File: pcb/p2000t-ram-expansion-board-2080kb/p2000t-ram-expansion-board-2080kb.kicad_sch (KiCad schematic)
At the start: 30 parts, among them J1 EXPANSION BOARD, J2 POWER, J3 TERMINAL, U1 74HC04, U10 AS6C4008-55PCN, U11 AS6C4008-55PCN, U12 74HC138, U13 74HC74, U2 AS6C4008-55PCN, U3 74HC00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

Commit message: Adding gerbers
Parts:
- added C14: 0.1uF, Capacitor_THT:C_Disc_D5.0mm_W2.5mm_P5.00mm, symbol Device:C
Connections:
- net +5V: now also C14.1
- net GND: now also C14.2
- no-connect marks 18 -> 17
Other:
- note added: "Currently not used"
- note added: "Port number 0x94 or 0x95 select D-type flip-flop 0x94 = 1001 0100 0x95 = 1001 0101"
- note added: "Writeable on port 0x94"
- note added: "Writeable on port 0x95"
- note removed: "Port number 0x94 selects D-type flip-flop 0x94 = 1001 0100"
- moved on the sheet: C2, U13A, U13B, U1A, U1D, U1E, U3B, U4, U6A

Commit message: Fixing bug in wiring
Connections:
- net A0: now also U3.4; no longer U1.11
- net GND: now also U1.11
- net at U1.10: no longer U3.4
- no-connect marks 17 -> 18
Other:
- note added: "0x94 | 0x95"
- note removed: "0x94"
- moved on the sheet: U1D, U1E
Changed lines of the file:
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@@
   (junction (at 113.03 85.09) (diameter 0) (color 0 0 0 0)
   )
+  (junction (at 91.44 53.975) (diameter 0) (color 0 0 0 0)
+  )
   (junction (at 93.98 59.055) (diameter 0) (color 0 0 0 0)
   )
@@
   )
   (no_connect (at 46.355 80.645))
+  (no_connect (at 144.78 224.79))
   (no_connect (at 237.49 163.195))
   (no_connect (at 33.655 75.565))
@@
     (stroke (width 0) (type default))
   )
-  (wire (pts (xy 217.17 51.435) (xy 217.17 46.355))
-    (stroke (width 0) (type default))
-  )
   (wire (pts (xy 239.395 109.855) (xy 239.395 123.19))
     (stroke (width 0) (type default))
@@
     (stroke (width 0) (type default))
   )
-  (wire (pts (xy 217.17 46.355) (xy 219.71 46.355))
-    (stroke (width 0) (type default))
-  )
   (polyline (pts (xy 200.66 89.535) (xy 177.165 89.535))
     (stroke (width 0) (type default))
@@
     (stroke (width 0) (type default))
   )
+  (wire (pts (xy 91.44 31.115) (xy 100.33 31.115))
+    (stroke (width 0) (type default))
+  )
   (wire (pts (xy 37.465 93.98) (xy 40.64 93.98))
     (stroke (width 0) (type default))
@@
     (stroke (width 0) (type default))
   )
-  (wire (pts (xy 234.95 38.1) (xy 234.95 46.355))
+  (wire (pts (xy 234.95 38.1) (xy 230.505 38.1))
     (stroke (width 0) (type default))
   )
@@
     (stroke (width 0) (type default))
   )
+  (wire (pts (xy 91.44 53.975) (xy 91.44 31.115))
+    (stroke (width 0) (type default))
+  )
   (wire (pts (xy 243.84 109.855) (xy 239.395 109.855))
     (stroke (width 0) (type default))
@@
     (effects (font (size 1.27 1.27)) (justify left bottom))
   )
-  (text "0x94" (at 90.678 64.516 90)
+  (text "0x94 | 0x95" (at 90.17 67.945 90)
     (effects (font (size 1.27 1.27)) (justify left bottom))
   )
@@
     )
   )
-  (global_label "A0" (shape input) (at 219.71 33.02 180) (fields_autoplaced)
+  (global_label "A0" (shape input) (at 234.95 33.02 180) (fields_autoplaced)
     (effects (font (size 1 1)) (justify right))
-    (property "Intersheetrefs" "${INTERSHEET_REFS}" (at 216.0005 32.9575 0)
+    (property "Intersheetrefs" "${INTERSHEET_REFS}" (at 231.2405 32.9575 0)
       (effects (font (size 1 1)) (justify right) hide)
     )
@@
     )
   )
-  (global_label "~{P=R}" (shape input) (at 217.17 51.435 270) (fields_autoplaced)
+  (global_label "~{P=R}" (shape input) (at 215.265 38.1 180) (fields_autoplaced)
     (effects (font (size 1.27 1.27)) (justify right))
-    (property "Intersheetrefs" "${INTERSHEET_REFS}" (at 217.17 58.5326 90)
+    (property "Intersheetrefs" "${INTERSHEET_REFS}" (at 208.1674 38.1 0)
       (effects (font (size 1.27 1.27)) (justify right) hide)
     )
@@
     )
   )
-  (symbol (lib_id "power:GND") (at 100.33 31.115 270) (unit 1)
-    (in_bom yes) (on_board yes) (dnp no) (fields_autoplaced)
-    (property "Reference" "#PWR065" (at 93.98 31.115 0)
-      (effects (font (size 1.27 1.27)) hide)
-    )
-    (property "Value" "GND" (at 96.52 31.115 90)
-      (effects (font (size 1.27 1.27)) (justify right))
-    )
-    (property "Footprint" "" (at 100.33 31.115 0)
-      (effects (font (size 1.27 1.27)) hide)
-    )
-    (property "Datasheet" "" (at 100.33 31.115 0)
-      (effects (font (size 1.27 1.27)) hide)
-    )
-    (pin "1")
-    (instances
-      (project "p2000t-ram-expansion-board-2080kb"
-        (path "/aa790391-403a-4556-8f28-ee78862c61e8"
-          (reference "#PWR065") (unit 1)
-        )
-      )
-    )
-  )
   (symbol (lib_id "power:GND") (at 291.465 60.96 180) (unit 1)
     (in_bom yes) (on_board yes) (dnp no) (fields_autoplaced)
@@
     )
   )
+  (symbol (lib_id "power:GND") (at 129.54 224.79 270) (unit 1)
+    (in_bom yes) (on_board yes) (dnp no)
+    (property "Reference" "#PWR071" (at 123.19 224.79 0)
+      (effects (font (size 1.27 1.27)) hide)
+    )
+    (property "Value" "GND" (at 121.92 224.79 90)
+      (effects (font (size 1.27 1.27)) (justify left))
+    )
+    (property "Footprint" "" (at 129.54 224.79 0)
+      (effects (font (size 1.27 1.27)) hide)
+    )
+    (property "Datasheet" "" (at 129.54 224.79 0)
+      (effects (font (size 1.27 1.27)) hide)
+    )
+    (pin "1")
+    (instances
+      (project "p2000t-ram-expansion-board-2080kb"
+        (path "/aa790391-403a-4556-8f28-ee78862c61e8"
+          (reference "#PWR071") (unit 1)
+        )
+      )
+    )
+  )
   (symbol (lib_id "74xx:74HC00") (at 242.57 35.56 0) (unit 2)
     (in_bom yes) (on_board yes) (dnp no)
@@
     )
   )
-  (symbol (lib_id "74xx:74HC04") (at 227.33 33.02 0) (unit 5)
+  (symbol (lib_id "74xx:74HC04") (at 137.16 224.79 0) (unit 5)
     (in_bom yes) (on_board yes) (dnp no)
-    (property "Reference" "U1" (at 220.98 36.195 0)
+    (property "Reference" "U1" (at 130.81 227.965 0)
       (effects (font (size 1.27 1.27)))
     )
-    (property "Value" "74HC04" (at 231.14 36.195 0)
+    (property "Value" "74HC04" (at 140.97 227.965 0)
       (effects (font (size 1.27 1.27)))
     )
-    (property "Footprint" "Package_DIP:DIP-14_W7.62mm_Socket" (at 227.33 33.02 0)
+    (property "Footprint" "Package_DIP:DIP-14_W7.62mm_Socket" (at 137.16 224.79 0)
       (effects (font (size 1.27 1.27)) hide)
     )
-    (property "Datasheet" "https://assets.nexperia.com/documents/data-sheet/74HC_HCT04.pdf" (at 227.33 33.02 0)
+    (property "Datasheet" "https://assets.nexperia.com/documents/data-sheet/74HC_HCT04.pdf" (at 137.16 224.79 0)
       (effects (font (size 1.27 1.27)) hide)
     )
@@
     )
   )
-  (symbol (lib_id "74xx:74HC04") (at 227.33 46.355 0) (unit 4)
+  (symbol (lib_id "74xx:74HC04") (at 222.885 38.1 0) (unit 4)
     (in_bom yes) (on_board yes) (dnp no)
-    (property "Reference" "U1" (at 220.98 42.545 0)
+    (property "Reference" "U1" (at 216.535 34.29 0)
       (effects (font (size 1.27 1.27)))
     )
-    (property "Value" "74HC04" (at 230.505 43.18 0)
+    (property "Value" "74HC04" (at 226.06 34.925 0)
       (effects (font (size 1.27 1.27)))
     )
-    (property "Footprint" "Package_DIP:DIP-14_W7.62mm_Socket" (at 227.33 46.355 0)
+    (property "Footprint" "Package_DIP:DIP-14_W7.62mm_Socket" (at 222.885 38.1 0)
       (effects (font (size 1.27 1.27)) hide)
     )
-    (property "Datasheet" "https://assets.nexperia.com/documents/data-sheet/74HC_HCT04.pdf" (at 227.33 46.355 0)
+    (property "Datasheet" "https://assets.nexperia.com/documents/data-sheet/74HC_HCT04.pdf" (at 222.885 38.1 0)
       (effects (font (size 1.27 1.27)) hide)
     )

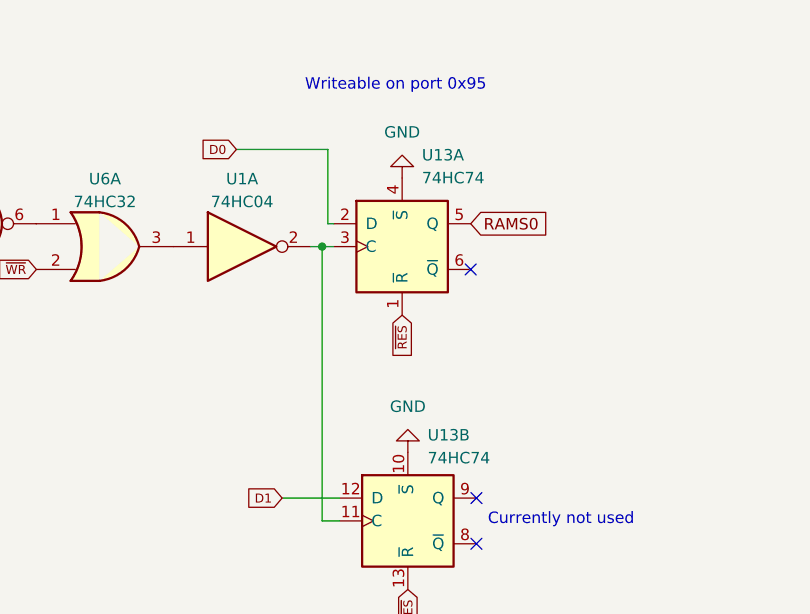
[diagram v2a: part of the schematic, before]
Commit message: Fixing another bug 74HC74
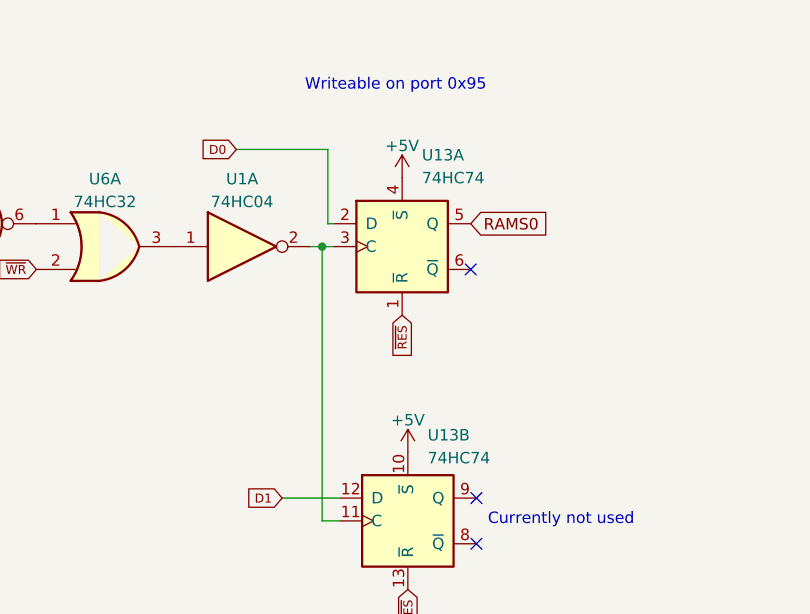
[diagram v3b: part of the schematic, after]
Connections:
- net +5V: now also U13.10 (~{S}), U13.4 (~{S})
- net GND: no longer U13.10 (~{S}), U13.4 (~{S})
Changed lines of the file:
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@@
-    )
-  )
-  (symbol (lib_id "power:GND") (at 291.465 60.96 180) (unit 1)
-    (in_bom yes) (on_board yes) (dnp no) (fields_autoplaced)
-    (property "Reference" "#PWR066" (at 291.465 54.61 0)
-      (effects (font (size 1.27 1.27)) hide)
-    )
-    (property "Value" "GND" (at 291.465 55.88 0)
-      (effects (font (size 1.27 1.27)))
-    )
-    (property "Footprint" "" (at 291.465 60.96 0)
-      (effects (font (size 1.27 1.27)) hide)
-    )
-    (property "Datasheet" "" (at 291.465 60.96 0)
-      (effects (font (size 1.27 1.27)) hide)
-    )
-    (pin "1")
-    (instances
-      (project "p2000t-ram-expansion-board-2080kb"
-        (path "/aa790391-403a-4556-8f28-ee78862c61e8"
-          (reference "#PWR066") (unit 1)
-        )
-      )
     )
   )
@@
         (path "/aa790391-403a-4556-8f28-ee78862c61e8"
           (reference "#PWR02") (unit 1)
-        )
-      )
-    )
-  )
-  (symbol (lib_id "power:GND") (at 290.83 30.48 180) (unit 1)
-    (in_bom yes) (on_board yes) (dnp no) (fields_autoplaced)
-    (property "Reference" "#PWR064" (at 290.83 24.13 0)
-      (effects (font (size 1.27 1.27)) hide)
-    )
-    (property "Value" "GND" (at 290.83 25.4 0)
-      (effects (font (size 1.27 1.27)))
-    )
-    (property "Footprint" "" (at 290.83 30.48 0)
-      (effects (font (size 1.27 1.27)) hide)
-    )
-    (property "Datasheet" "" (at 290.83 30.48 0)
-      (effects (font (size 1.27 1.27)) hide)
-    )
-    (pin "1")
-    (instances
-      (project "p2000t-ram-expansion-board-2080kb"
-        (path "/aa790391-403a-4556-8f28-ee78862c61e8"
-          (reference "#PWR064") (unit 1)
         )
       )
@@
     )
   )
+  (symbol (lib_id "power:+5V") (at 291.465 60.96 0) (unit 1)
+    (in_bom yes) (on_board yes) (dnp no) (fields_autoplaced)
+    (property "Reference" "#PWR065" (at 291.465 64.77 0)
+      (effects (font (size 1.27 1.27)) hide)
+    )
+    (property "Value" "+5V" (at 291.465 57.3842 0)
+      (effects (font (size 1.27 1.27)))
+    )
+    (property "Footprint" "" (at 291.465 60.96 0)
+      (effects (font (size 1.27 1.27)) hide)
+    )
+    (property "Datasheet" "" (at 291.465 60.96 0)
+      (effects (font (size 1.27 1.27)) hide)
+    )
+    (pin "1")
+    (instances
+      (project "p2000t-ram-expansion-board-2080kb"
+        (path "/aa790391-403a-4556-8f28-ee78862c61e8"
+          (reference "#PWR065") (unit 1)
+        )
+      )
+    )
+  )
   (symbol (lib_id "74xx:74HC74") (at 290.83 38.1 0) (unit 1)
     (in_bom yes) (on_board yes) (dnp no)
@@
         )
       )
+    )
+  )
+  (symbol (lib_id "power:+5V") (at 290.83 30.48 0) (unit 1)
+    (in_bom yes) (on_board yes) (dnp no) (fields_autoplaced)
+    (property "Reference" "#PWR064" (at 290.83 34.29 0)
+      (effects (font (size 1.27 1.27)) hide)
+    )
+    (property "Value" "+5V" (at 290.83 26.9042 0)
+      (effects (font (size 1.27 1.27)))
+    )
+    (property "Footprint" "" (at 290.83 30.48 0)
+      (effects (font (size 1.27 1.27)) hide)
+    )
+    (property "Datasheet" "" (at 290.83 30.48 0)
+      (effects (font (size 1.27 1.27)) hide)
+    )
+    (pin "1")
+    (instances
+      (project "p2000t-ram-expansion-board-2080kb"
+        (path "/aa790391-403a-4556-8f28-ee78862c61e8"
+          (reference "#PWR064") (unit 1)
+        )
+      )

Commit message: Revising PCBs
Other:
- title: P2000T RAM expansion board -> Philips P2000T Memory Expansion 2Mb+
